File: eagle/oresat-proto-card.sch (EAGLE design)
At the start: 62 parts, among them J1 J-SAMTEC-TFM-110-X1-XXX-D-RA, J2 U.FL, J3 U.FL, J4 U.FL, J6 J-SAMTEC-TFM-120-X1-XXX-D-RA, J7 1.27MM-SWD-CONNECTOR, U1 TPS63070, U2 TCAN330, U6 STM32F042K6, X1 16MHZ-2.5x2mm

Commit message: Uh. Yeah. Well, it wasn't my fault, I blame Oliver J. Power domain circuitry now figured out from a topology point of view. Lots of changes to the power front end, and the main and aux connctors. Also, added the beginnings of design markdown file.
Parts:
- removed C14: 22u, oresat-rcl:C-EU0603-B-NOSILK
- removed C18, C25: 22u, oresat-rcl:C-EU0805-B-NOSILK
- removed C6, C8: 10u, oresat-rcl:C-EU0805-B-NOSILK
- removed JP7: (no value), pinhead:PINHD-1X5
- removed L3: 1.5 uH, L-Coilcraft-XFL4020:L-COILCRAFT-XFL4020
- removed R12: 150k, rcl_custom:R-US_0402-B-NOSILK
- removed R15: 10k, rcl_custom:R-US_0402-B-NOSILK
- removed R16, R18: NP, rcl_custom:R-US_0402-B-NOSILK
- removed TP2, TP3, TP4, TP5: TEST-POINT, Tova:TEST-POINT
- removed U1: TPS63070, ic-pwr-tps63070x:TPS63070X
- added C1: 100n, rcl_custom:C-EU0402-B-NOSILK
- added C10: 1u, oresat-rcl:C-EU0603-B-NOSILK
- added C12: 22u, oresat-rcl:C-EU0805-B-NOSILK
- added C2: TBD, rcl_custom:C-EU0402-B-NOSILK
- added C7: 10u, oresat-rcl:C-EU0805-B-NOSILK
- added IC1: (no value), v-reg:XC63FPM
- added L2: 6.8u, L-ECS-MPI4040:L-ECS-MPI4040
- added Q3, Q4: MOSFET-PCH-SOT23-6, Q-MOSFET-PCH-SOT23-6:MOSFET-PCH-SOT23-6
- added Q5, Q6: PMV45EN, Tova:PMV45EN
- added R11, R13, R14, R19, R20, R21, R22, R23, R5, R6, R8, R9: NP, rcl_custom:R-US_0402-B-NOSILK
- added R24, R25, R31, R32, R33, R34, R36, R37, R4: TBD, rcl_custom:R-US_0402-B-NOSILK
- added R26, R27, R28, R30, R35, R38: 10K, rcl_custom:R-US_0402-B-NOSILK
- added R29: (no value), rcl:R-US_R1206
- added TP11, TP12, TP13, TP14, TP16, TP17, TP19, TP6, TP7, TP8, TP9: TEST-POINT, Tova:TEST-POINT
- added U3: MAX7310, U-Maxim-MAX7310-I2C-GPIO-expander:MAX7310
- added U4: MAX4211, U-Maxim-MAX4211-power-monitor:MAX4211
- added U5: TPS62111, U-TI-TPS6211x-SPS-buck:TPS6211X
- C4: value 10u -> 1u
- C5: value 100n -> 1u; device rcl_custom:C-EU0402-B-NOSILK -> oresat-rcl:C-EU0603-B-NOSILK
- R10: value 470k -> NP
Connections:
- removed net SPARE10: J6.1, J6.2, JP11.2
- removed net SPARE8: J6.5, J6.6, JP11.4
- removed net SPARE9: J6.3, J6.4, JP11.1
- removed net TPS-EN1: R18.2, R7.1, TP5.1, U1.EN, U1.PS/SYNC
- removed net TPS-FB1: R10.1, R12.2, U1.FB
- removed net TPS-FB3: TP3.1, U1.FB2
- removed net TPS-L3: L3.1, U1.L1
- removed net TPS-L4: L3.2, U1.L2
- removed net TPS-PG1: R16.1, TP2.1, U1.PG
- removed net TPS-VAUX1: C5.1, U1.VAUX
- removed net TPS-VSEL1: R15.2, TP4.1, U1.VSEL
- new net !FAULT: Q6.D, R38.1, TP8.1, U3.IO2
- new net AD0: R5.1, R6.2, R8.2, R9.1, U3.AD0
- new net AD1: R11.1, R13.2, R14.2, R19.1, U3.AD1
- new net AD2: R20.1, R21.2, R22.2, R23.1, U3.AD2
- new net CB-RESET: R30.2, TP14.1, U3.IO1, U4.CIN2-
- new net CB_CTRL: Q3.G, Q6.G, R35.1, U4.COUT1, U4.COUT2, U4.LE
- new net N$398: C4.1, IC1.IN, Q3.S, R29.2, R35.2, U4.RS-
- new net N$585: C5.1, IC1.OUT, U4.VCC
- new net N$589: R26.1, U3.!RESET
- new net N$590: Q4.G, Q5.D, R27.1
- new net N$593: Q4.D, R29.1, U4.RS+
- new net N$596: R31.1, R32.2, TP12.1, U4.CIN1-
- new net N$597: R33.1, R34.2, TP11.1, U4.CIN1+
- new net N$598: R31.2, TP7.1, U4.IOUT
- new net N$599: R33.2, U4.CIN2+, U4.REF
- new net N$600: TP6.1, U4.POUT
- new net N$603: C2.1, R36.2, R37.2
- new net N$604: R37.1, U4.INHIBIT
- new net ON/!OFF: Q5.G, R28.2, TP13.1, U3.IO0
- new net OPD_PWR: J6.19, J6.20, R4.1
- new net OPD_SCL: J6.17, J6.18, R24.1
- new net OPD_SDA: J6.15, J6.16, R25.1
- new net PEN-SCL-FILT: R13.1, R21.1, R24.2, R6.1, U3.SCL
- new net PEN-SDA-FILT: R19.2, R23.2, R25.2, R9.2, U3.SDA
- new net TPS62111-PG: TP16.1, U5.PG
- new net TPS62111-SYNC: R10.2, R7.1, TP19.1, U5.SYNC
- new net TPS62111_SW: L2.1, U5.SW
- new net VBUSP: C10.1, C2.2, C7.1, JP1.5, JP3.1, JP3.2, JP3.3, JP8.1, Q3.D, R1.2, R7.2, TP9.1, U5.EN, U5.VIN
- new net VPD: C1.2, R11.2, R20.2, R26.2, R38.2, R4.2, R5.2, TP1.1, U3.V+
- net 3.3V: now also C12.1, L2.2, TP17.1, U5.FB; no longer C14.1, C18.1, C25.1, R10.2, R16.2, TP1.1, U1.VOUT
- net GND: now also C1.1, C10.2, C12.2, C7.2, IC1.GND, JP11.10, JP11.9, Q5.S, Q6.S, R10.1, R14.1, R22.1, R28.1, R30.1, R32.1, R34.1, R36.1, R8.1, U3.GND, U4.GND, U5.GND, U5.LBI, U5.LBO; no longer C14.2, C18.2, C25.2, C6.2, C8.2, R12.1, R15.1, R18.1, U1.GND, U1.PGND
- net SPARE1: now also J6.13, J6.14, JP11.8; no longer J6.19, J6.20, JP11.10
- net SPARE2: now also J6.11, J6.12, JP11.7; no longer J6.17, J6.18, JP11.9
- net SPARE3: now also J6.10, J6.9, JP11.6; no longer J6.15, J6.16, JP11.7
- net SPARE4: now also J6.7, J6.8, JP11.5; no longer J6.13, J6.14, JP11.8
- net SPARE5: now also J6.5, J6.6, JP11.4; no longer J6.11, J6.12, JP11.5
- net SPARE6: now also J6.3, J6.4, JP11.3; no longer J6.10, J6.9, JP11.6
- net SPARE7: now also J6.1, J6.2, JP11.2; no longer J6.7, J6.8, JP11.3
- net VBUS: now also Q4.S, R27.2; no longer C4.1, C6.1, C8.1, JP1.5, JP3.1, JP3.2, JP3.3, JP7.1, JP7.2, JP7.3, JP7.4, JP7.5, JP8.1, R1.2, R7.2, U1.VIN
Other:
- note added: "(3.3V)"
- note added: "(From power domain pins)"
- note added: "3.1"
- note added: "3.3V Card Switching Supply"
- note added: "Address selection for Card (See MAX7310 datasheet)"
- note added: "Breakouts"
- note added: "Card Power Switch and Circuit Breaker"
- note added: "ECS-MPI4040R4-6R8-R"
- note added: "FTDI TTL-232R-3V3 cable"
- note added: "Main Power Switch"
- note added: "OreSat Power Domain (OPD) Controller"
- note added: "OreSat Power Domain (OPD) Power Supply (3.3V)"
- note added: "OreSat Power Domain signals (See power sheet)"
- note added: "OreSat Power Enable (PEN)"
- note added: "TBD"
- note added: "Vbus = (6.0,7.2,8.4)V"
- note removed: "2.0"
- note removed: "Meant for FTDI TTL-232R-3V3 cable"
- note removed: "Vbus = (3.0, 3.6, 4.2) V"

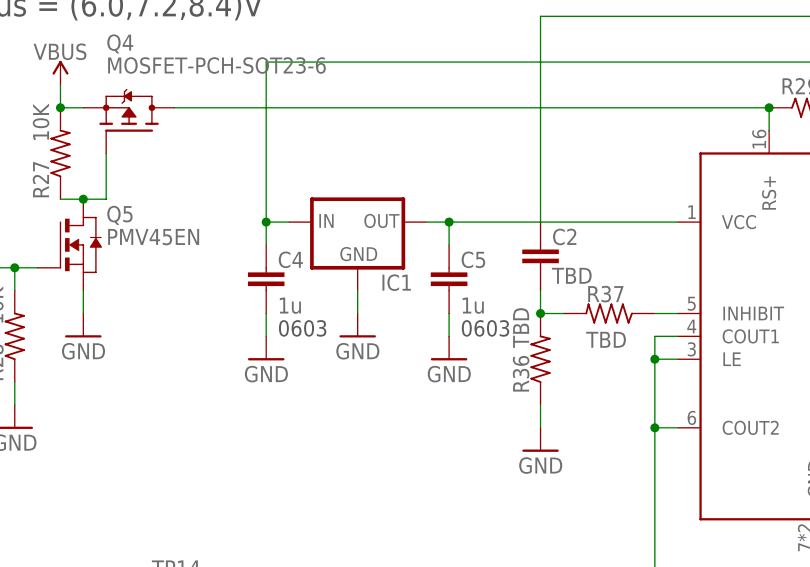
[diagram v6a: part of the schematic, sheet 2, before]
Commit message: Cleaned up TNAMES layer.
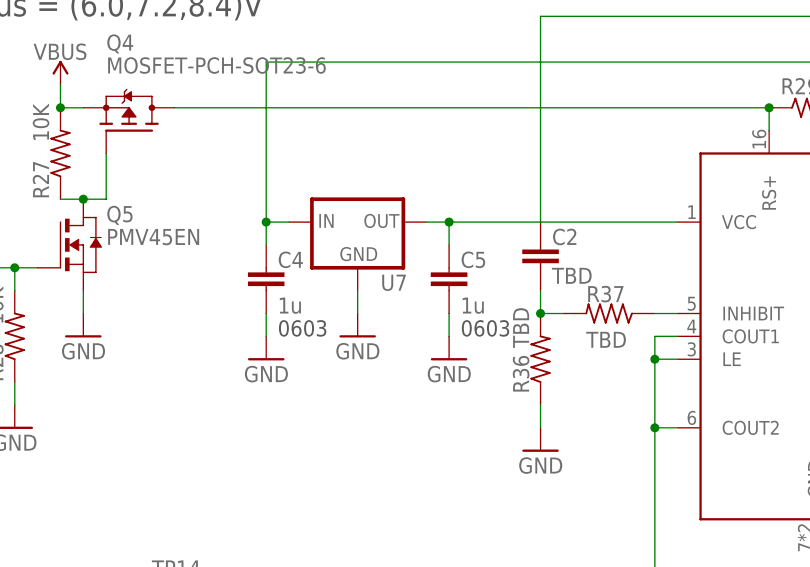
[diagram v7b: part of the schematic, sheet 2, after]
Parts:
- renumbered IC1 to U7
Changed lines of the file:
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@@
 <setting verticaltext="up"/>
 </settings>
-<grid distance="0.05" unitdist="inch" unit="inch" style="lines" multiple="2" display="yes" altdistance="0.01" altunitdist="inch" altunit="inch"/>
+<grid distance="0.1" unitdist="inch" unit="inch" style="lines" multiple="1" display="no" altdistance="0.01" altunitdist="inch" altunit="inch"/>
 <layers>
 <layer number="1" name="Top" color="4" fill="1" visible="no" active="no"/>
@@
 <part name="Q5" library="Tova" deviceset="PMV45EN" device=""/>
 <part name="Q6" library="Tova" deviceset="PMV45EN" device=""/>
-<part name="IC1" library="v-reg" library_urn="urn:adsk.eagle:library:409" deviceset="XC63FP" device="M" package3d_urn="urn:adsk.eagle:package:30367/1"/>
+<part name="U7" library="v-reg" library_urn="urn:adsk.eagle:library:409" deviceset="XC63FP" device="M" package3d_urn="urn:adsk.eagle:package:30367/1"/>
 <part name="C4" library="oresat-rcl" deviceset="C-EU" device="0603-B-NOSILK" value="1u">
 <attribute name="DIS" value="Digi-Key"/>
@@
 <attribute name="NAME" x="363.22" y="167.64" size="1.778" layer="95"/>
 </instance>
-<instance part="IC1" gate="G$1" x="233.68" y="185.42" smashed="yes">
+<instance part="U7" gate="G$1" x="233.68" y="185.42" smashed="yes">
 <attribute name="NAME" x="236.22" y="177.8" size="1.778" layer="95"/>
 <attribute name="VALUE" x="236.22" y="175.26" size="1.778" layer="96"/>
@@
 <segment>
 <pinref part="GND44" gate="1" pin="GND"/>
-<pinref part="IC1" gate="G$1" pin="GND"/>
+<pinref part="U7" gate="G$1" pin="GND"/>
 <wire x1="233.68" y1="175.26" x2="233.68" y2="177.8" width="0.1524" layer="91"/>
 </segment>
@@
 <pinref part="C5" gate="CE" pin="1"/>
 <wire x1="243.84" y1="182.88" x2="243.84" y2="185.42" width="0.1524" layer="91"/>
-<pinref part="IC1" gate="G$1" pin="OUT"/>
+<pinref part="U7" gate="G$1" pin="OUT"/>
 <wire x1="243.84" y1="185.42" x2="241.3" y2="185.42" width="0.1524" layer="91"/>
 <pinref part="U4" gate="G$1" pin="VCC"/>
@@
 <segment>
 <pinref part="C4" gate="CE" pin="1"/>
-<pinref part="IC1" gate="G$1" pin="IN"/>
+<pinref part="U7" gate="G$1" pin="IN"/>
 <wire x1="223.52" y1="185.42" x2="226.06" y2="185.42" width="0.1524" layer="91"/>
 <wire x1="223.52" y1="185.42" x2="223.52" y2="182.88" width="0.1524" layer="91"/>
